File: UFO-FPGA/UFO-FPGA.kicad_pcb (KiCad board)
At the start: 2 copper layers, 68.6 x 53.3 mm, 12 parts, among them J1 Power, J2 Analog, J3 Digital/PWM, J4 Digital/PWM, U1 ICE40HX8K-BG121, U2 FT2232HL, U3 ASDMB-12MHz

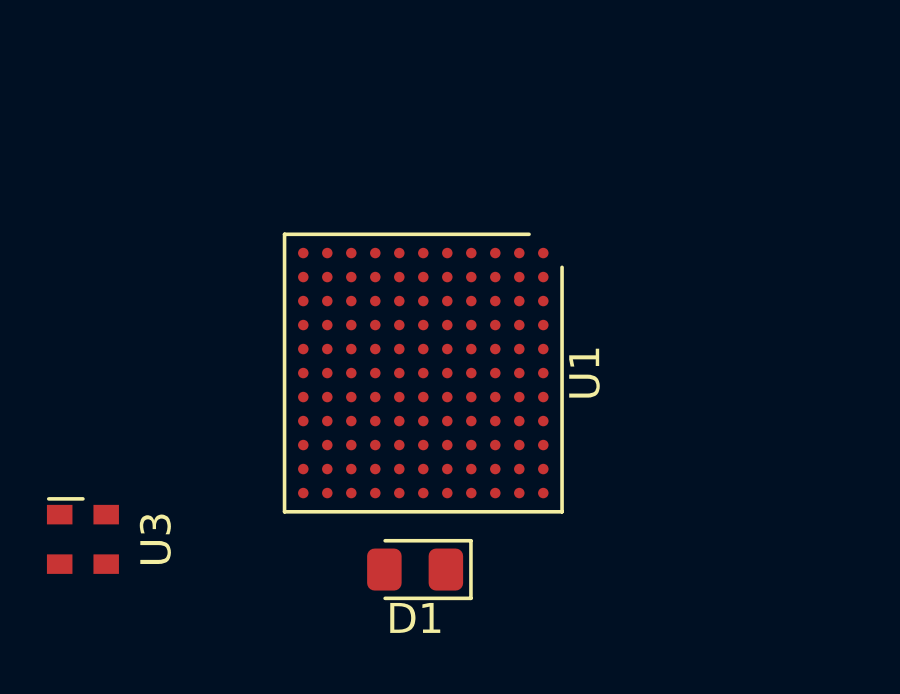
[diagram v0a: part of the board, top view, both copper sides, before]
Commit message: pins and USB
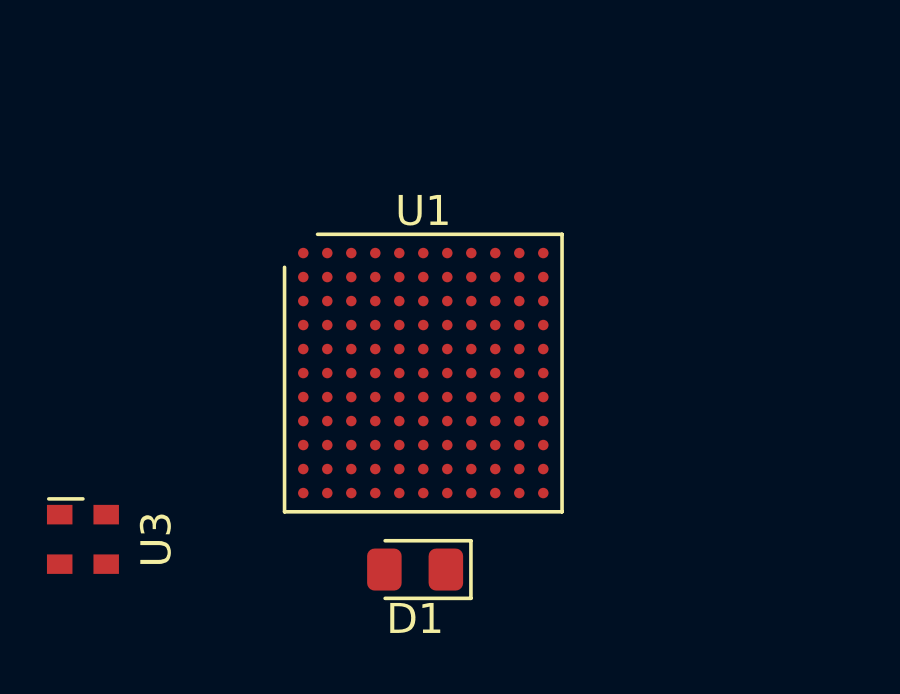
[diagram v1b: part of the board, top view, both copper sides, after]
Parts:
- turned U1 to 0 degrees
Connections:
- U1 pad A4: unconnected-(U1A-IOT_211-PadA4) -> MISO
- U1 pad A5: CHSEL -> ADC-CS
- U1 pad A6: ADC-CS -> SCK
- U1 pad B5: MISO -> CHSEL
- U1 pad B6: SCK -> unconnected-(U1A-IOT_198_GBIN0-PadB6)
- U1 pad G1: unconnected-(U1D-IOL_14A_GBIN6-PadG1) -> ICE_CLK

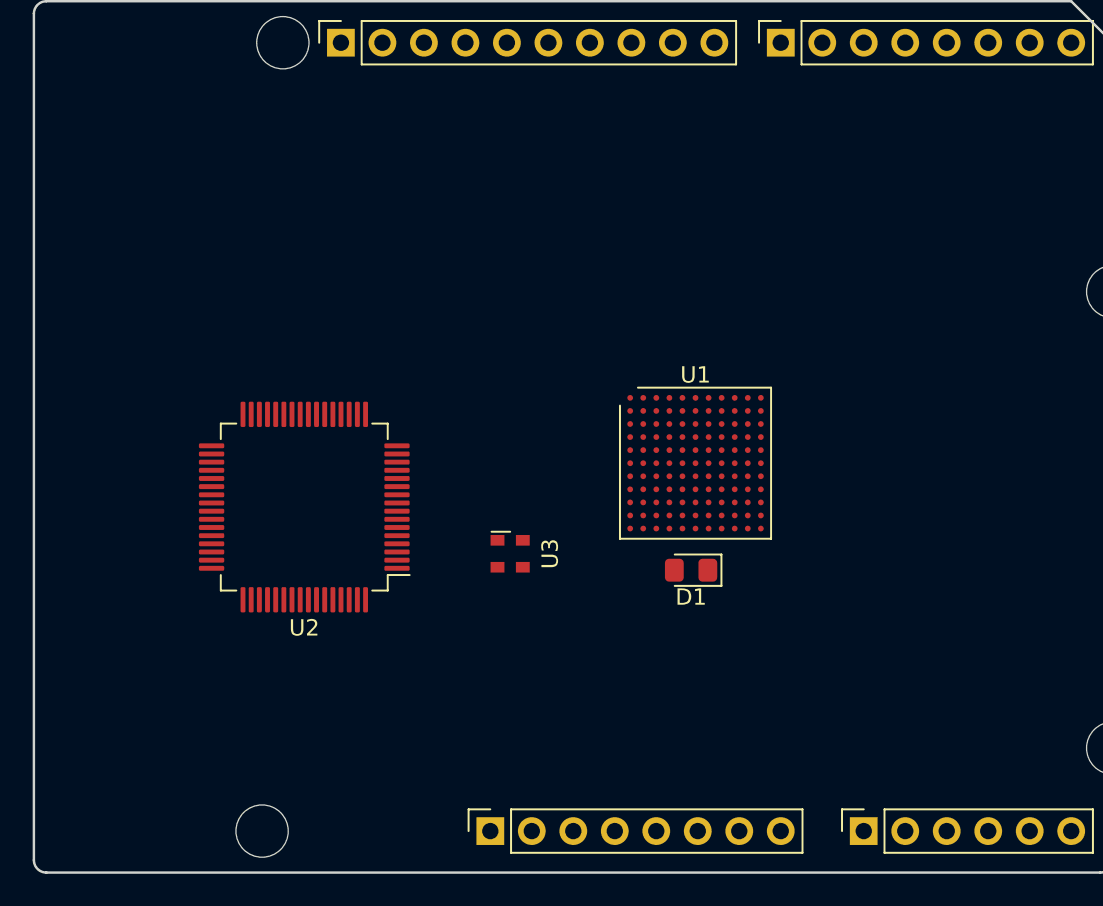
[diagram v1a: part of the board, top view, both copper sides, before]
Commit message: PCB and footprint
Added foorprints and moved on pcb layout
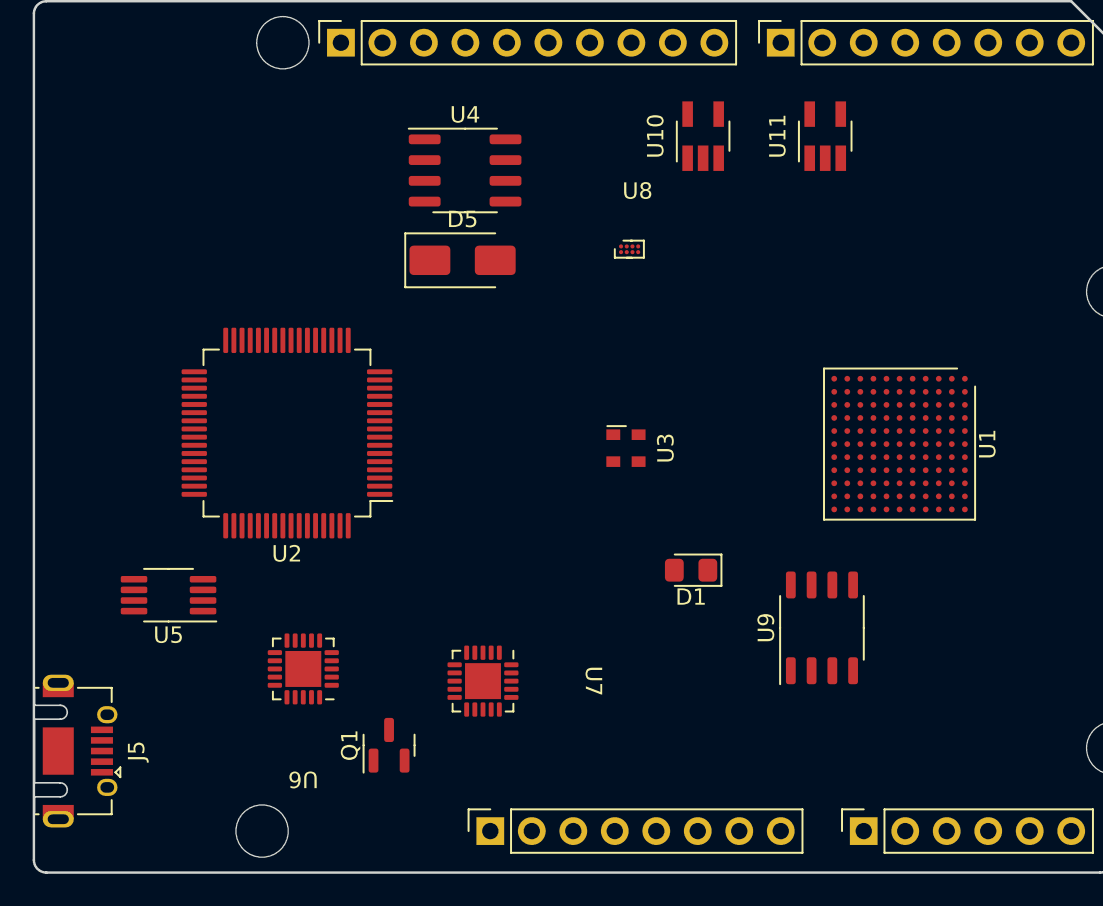
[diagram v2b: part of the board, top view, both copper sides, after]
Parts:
- added D5: B140-E3, Diode_SMD:D_SMA, F.Cu at (137.8, 64.0)
- added J5: USB_B_Micro, Connector_USB:USB_Micro-AB_Molex_47590-0001, F.Cu at (113.0, 94.0)
- added Q1: 2N7002, Package_TO_SOT_SMD:SOT-23, F.Cu at (133.2, 93.7)
- added U10: TL071, Package_TO_SOT_SMD:SOT-23-5_HandSoldering, F.Cu at (152.5, 56.4)
- added U11: TL071, Package_TO_SOT_SMD:SOT-23-5_HandSoldering, F.Cu at (159.9, 56.4)
- added U4: MC34063AD, Package_SO:SOIC-8_3.9x4.9mm_P1.27mm, F.Cu at (137.9, 58.5)
- added U5: 93LC56CT-I/MS, Package_SO:MSOP-8_3x3mm_P0.65mm, F.Cu at (119.8, 84.5)
- added U6: PWR convert, UFO-Footpints:W-QFN3535-20, F.Cu at (128.0, 95.3)
- added U7: PWR convert, UFO-Footpints:W-QFN3535-20, F.Cu at (145.3, 89.8)
- added U8: ADC, UFO-Footpints:WLP-8, F.Cu at (152.1, 57.2)
- added U9: N25Q032A13ESC40F, Package_SO:SOP-8_3.9x4.9mm_P1.27mm, F.Cu at (159.8, 86.5)
- J2: value Analog -> Digital
- J4: value Digital/PWM -> Digital
- moved U1 12.5 mm to (164.5, 75.2), turned to -90 degrees
- moved U3 9.59 mm to (147.8, 75.5)
- moved U2 4.65 mm to (127.0, 74.6)
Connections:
- net /USB Programmer/Prog-REF renamed Net-(U2-REF)
- net /USB Programmer/Prog-RESET renamed Net-(U2-~{RESET})
- J1 pad 2: /PINOUT/IOREF -> PIN-22
- J1 pad 3: /PINOUT/~{RESET} -> PIN-23
- J1 pad 8: VCC -> Vin
- J2 pad 1: /PINOUT/A0 -> PIN-18
- J2 pad 2: /PINOUT/A1 -> PIN-19
- J2 pad 3: /PINOUT/A2 -> PIN-20
- J2 pad 4: /PINOUT/A3 -> PIN-21
- J2 pad 5: /PINOUT/SDA/A4 -> AIN1
- J2 pad 6: /PINOUT/SCL/A5 -> AIN2
- J3 pad 1: /PINOUT/SCL/A5 -> PIN-1
- J3 pad 2: /PINOUT/SDA/A4 -> PIN-2
- J3 pad 3: /PINOUT/AREF -> PIN-3
- J3 pad 5: /PINOUT/13 -> PIN-4
- J3 pad 6: /PINOUT/12 -> PIN-5
- J4 pad 1: /PINOUT/7 -> PIN-10
- J4 pad 2: /PINOUT/*6 -> PIN-11
- J4 pad 3: /PINOUT/*5 -> PIN-12
- J4 pad 4: /PINOUT/4 -> PIN-13
- J4 pad 5: /PINOUT/*3 -> PIN-14
- J4 pad 6: /PINOUT/2 -> PIN-15
- J4 pad 7: /PINOUT/TX/1 -> PIN-16
- J4 pad 8: /PINOUT/RX/0 -> PIN-17
- U1 pad A1: unconnected-(U1A-IOT_225-PadA1) -> PIN-1
- U1 pad A10: RS232_Tx_TTL -> unconnected-(U1A-IOT_170-PadA10)
- U1 pad A11: RS232_Rx_TTL -> unconnected-(U1A-IOT_168-PadA11)
- U1 pad A2: unconnected-(U1A-IOT_222-PadA2) -> PIN-3
- U1 pad A3: unconnected-(U1A-IOT_223-PadA3) -> PIN-2
- U1 pad A7: DCDn -> unconnected-(U1A-IOT_192-PadA7)
- U1 pad A8: DSRn -> unconnected-(U1A-IOT_190-PadA8)
- U1 pad A9: DTRn -> unconnected-(U1A-IOT_178-PadA9)
- U1 pad B1: unconnected-(U1D-IOL_2A-PadB1) -> PIN-9
- U1 pad B11: unconnected-(U1B-IOR_161-PadB11) -> PIN-23
- U1 pad B2: unconnected-(U1D-IOL_2B-PadB2) -> PIN-8
- U1 pad B3: unconnected-(U1A-IOT_221-PadB3) -> PIN-4
- U1 pad B4: unconnected-(U1A-IOT_219-PadB4) -> PIN-5
- U1 pad B6: unconnected-(U1A-IOT_198_GBIN0-PadB6) -> PIN-6
- U1 pad B7: unconnected-(U1A-IOT_197_GBIN1-PadB7) -> PIN-7
- U1 pad B8: CTSn -> unconnected-(U1A-IOT_177-PadB8)
- U1 pad B9: RTSn -> unconnected-(U1A-IOT_174-PadB9)
- U1 pad C11: unconnected-(U1B-IOR_160-PadC11) -> PIN-22
- U1 pad D11: unconnected-(U1B-IOR_152-PadD11) -> PIN-21
- U1 pad E10: unconnected-(U1B-IOR_141_GBIN2-PadE10) -> PIN-19
- U1 pad E11: unconnected-(U1B-IOR_148-PadE11) -> PIN-20
- U1 pad F10: unconnected-(U1B-IOR_136-PadF10) -> PIN-17
- U1 pad F11: unconnected-(U1B-IOR_140_GBIN3-PadF11) -> PIN-18
- U1 pad G10: unconnected-(U1B-IOR_120-PadG10) -> PIN-15
- U1 pad G11: unconnected-(U1B-IOR_129-PadG11) -> PIN-16
- U1 pad H10: unconnected-(U1B-IOR_116-PadH10) -> PIN-12
- U1 pad H11: unconnected-(U1B-IOR_119-PadH11) -> PIN-14
- U1 pad J10: unconnected-(U1B-IOR_117-PadJ10) -> PIN-13
- U1 pad J11: unconnected-(U1B-IOR_114-PadJ11) -> PIN-10
- U1 pad K1: unconnected-(U1D-IOL_23B-PadK1) -> RS232_Tx_TTL
- U1 pad K11: unconnected-(U1B-IOR_115-PadK11) -> PIN-11
- U1 pad L1: unconnected-(U1C-IOB_56-PadL1) -> RS232_Rx_TTL
- U1 pad L2: unconnected-(U1C-IOB_61-PadL2) -> RTSn
- U1 pad L3: unconnected-(U1C-IOB_71-PadL3) -> CTSn
- U1 pad L4: unconnected-(U1C-IOB_72-PadL4) -> DTRn
- U1 pad L5: unconnected-(U1C-IOB_81_GBIN5-PadL5) -> DSRn
- U1 pad L7: unconnected-(U1C-IOB_94-PadL7) -> DCDn

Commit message: edge cuts
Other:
- outline, holes or cut-outs redrawn
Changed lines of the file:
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@@
   )
   (footprint "Connector_USB:USB_Micro-AB_Molex_47590-0001" (layer "F.Cu")
-    (at 113 94.041 -90)
+    (at 112.951 94.041 -90)
     (descr "Micro USB AB receptable, right-angle inverted (https://www.molex.com/pdm_docs/sd/475900001_sd.pdf)")
     (tags "Micro AB USB SMD")
@@
   (gr_line (start 180.088 63.38) (end 180.088 97.67)
     (stroke (width 0.15) (type solid)) (layer "Edge.Cuts"))
-  (gr_line (start 111.508 100.718) (end 111.508 48.902)
+  (gr_line (start 111.508 100.718) (end 111.506 97.791)
     (stroke (width 0.15) (type solid)) (layer "Edge.Cuts"))
   (gr_line (start 177.548 100.21) (end 177.548 100.718)
@@
   (gr_arc (start 112.27 101.48) (mid 111.731185 101.256815) (end 111.508 100.718)
     (stroke (width 0.15) (type solid)) (layer "Edge.Cuts"))
+  (gr_line (start 111.501 90.291) (end 111.508 48.902)
+    (stroke (width 0.15) (type solid)) (layer "Edge.Cuts"))
   (gr_line (start 112.27 48.14) (end 175.008 48.14)

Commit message: footprints and PCB
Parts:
- added D2: GREEN, LED_SMD:LED_0805_2012Metric_Pad1.15x1.40mm_HandSolder, F.Cu at (37.5, 85.6)
- added D3: RXLED, LED_SMD:LED_0805_2012Metric_Pad1.15x1.40mm_HandSolder, F.Cu at (33.1, 71.6)
- added D4: TXLED, LED_SMD:LED_0805_2012Metric_Pad1.15x1.40mm_HandSolder, F.Cu at (33.1, 74.6)
- added D6: LED, LED_SMD:LED_0805_2012Metric_Pad1.15x1.40mm_HandSolder, F.Cu at (44.3, 79.7)
- added D7: POWER, LED_SMD:LED_0805_2012Metric_Pad1.15x1.40mm_HandSolder, F.Cu at (63.2, 53.9)
- added FB1: 600 Ohm, 500mA, Inductor_SMD:L_1206_3216Metric_Pad1.22x1.90mm_HandSolder, F.Cu at (59.5, 71.5)
- added R1: 2K2, Resistor_SMD:R_0805_2012Metric_Pad1.20x1.40mm_HandSolder, F.Cu at (33.1, 53.8)
- added R10: 0, Resistor_SMD:R_0805_2012Metric_Pad1.20x1.40mm_HandSolder, F.Cu at (37.8, 62.7)
- added R11: 0, Resistor_SMD:R_0805_2012Metric_Pad1.20x1.40mm_HandSolder, F.Cu at (37.8, 65.6)
- added R12: 0, Resistor_SMD:R_0805_2012Metric_Pad1.20x1.40mm_HandSolder, F.Cu at (37.8, 68.6)
- added R13: 0, Resistor_SMD:R_0805_2012Metric_Pad1.20x1.40mm_HandSolder, F.Cu at (42.6, 53.8)
- added R14: 0, Resistor_SMD:R_0805_2012Metric_Pad1.20x1.40mm_HandSolder, F.Cu at (42.6, 56.8)
- added R15: 0, Resistor_SMD:R_0805_2012Metric_Pad1.20x1.40mm_HandSolder, F.Cu at (42.6, 59.7)
- added R16: 0, Resistor_SMD:R_0805_2012Metric_Pad1.20x1.40mm_HandSolder, F.Cu at (42.6, 62.7)
- added R17: 0, Resistor_SMD:R_0805_2012Metric_Pad1.20x1.40mm_HandSolder, F.Cu at (42.6, 65.6)
- added R18: 0, Resistor_SMD:R_0805_2012Metric_Pad1.20x1.40mm_HandSolder, F.Cu at (42.6, 68.6)
- added R19: 0, Resistor_SMD:R_0805_2012Metric_Pad1.20x1.40mm_HandSolder, F.Cu at (47.3, 53.8)
- added R2: 10K, Resistor_SMD:R_0805_2012Metric_Pad1.20x1.40mm_HandSolder, F.Cu at (33.1, 56.8)
- added R20: 0, Resistor_SMD:R_0805_2012Metric_Pad1.20x1.40mm_HandSolder, F.Cu at (47.3, 56.8)
- added R21: 10K, Resistor_SMD:R_0805_2012Metric_Pad1.20x1.40mm_HandSolder, F.Cu at (54.1, 79.4)
- added R22: 10K, Resistor_SMD:R_0805_2012Metric_Pad1.20x1.40mm_HandSolder, F.Cu at (54.1, 82.4)
- added R23: 10K, Resistor_SMD:R_0805_2012Metric_Pad1.20x1.40mm_HandSolder, F.Cu at (54.1, 85.3)
- added R24: 10K, Resistor_SMD:R_0805_2012Metric_Pad1.20x1.40mm_HandSolder, F.Cu at (54.1, 88.3)
- added R25: 100, Resistor_SMD:R_0805_2012Metric_Pad1.20x1.40mm_HandSolder, F.Cu at (54.1, 91.2)
- added R26: 100, Resistor_SMD:R_0805_2012Metric_Pad1.20x1.40mm_HandSolder, F.Cu at (54.1, 94.2)
- added R27: 10K, Resistor_SMD:R_0805_2012Metric_Pad1.20x1.40mm_HandSolder, F.Cu at (37.4, 79.6)
- added R29: 1, Resistor_SMD:R_0805_2012Metric_Pad1.20x1.40mm_HandSolder, F.Cu at (37.4, 82.6)
- added R3: 10K, Resistor_SMD:R_0805_2012Metric_Pad1.20x1.40mm_HandSolder, F.Cu at (33.1, 59.7)
- added R30: 1, Resistor_SMD:R_0805_2012Metric_Pad1.20x1.40mm_HandSolder, F.Cu at (46.6, 90.5)
- added R31: 1, Resistor_SMD:R_0805_2012Metric_Pad1.20x1.40mm_HandSolder, F.Cu at (33.1, 90.5)
- added R32: 1, Resistor_SMD:R_0805_2012Metric_Pad1.20x1.40mm_HandSolder, F.Cu at (39.8, 90.5)
- added R33: 220R, Resistor_SMD:R_0805_2012Metric_Pad1.20x1.40mm_HandSolder, F.Cu at (47.3, 59.7)
- added R34: 220R, Resistor_SMD:R_0805_2012Metric_Pad1.20x1.40mm_HandSolder, F.Cu at (47.3, 62.7)
- added R35: 0, Resistor_SMD:R_0805_2012Metric_Pad1.20x1.40mm_HandSolder, F.Cu at (54.1, 53.8)
- added R36: 1K, Resistor_SMD:R_0805_2012Metric_Pad1.20x1.40mm_HandSolder, F.Cu at (54.1, 56.8)
- added R37: 12K4, Resistor_SMD:R_0805_2012Metric_Pad1.20x1.40mm_HandSolder, F.Cu at (54.1, 59.7)
- added R38: 24K9, Resistor_SMD:R_0805_2012Metric_Pad1.20x1.40mm_HandSolder, F.Cu at (54.1, 62.7)
- added R39: 100k, Resistor_SMD:R_0805_2012Metric_Pad1.20x1.40mm_HandSolder, F.Cu at (54.1, 65.6)
- added R4: 10K, Resistor_SMD:R_0805_2012Metric_Pad1.20x1.40mm_HandSolder, F.Cu at (33.1, 62.7)
- added R40: 1M, Resistor_SMD:R_0805_2012Metric_Pad1.20x1.40mm_HandSolder, F.Cu at (54.1, 68.6)
- added R41: 1M, Resistor_SMD:R_0805_2012Metric_Pad1.20x1.40mm_HandSolder, F.Cu at (54.1, 71.5)
- added R5: 2K2, Resistor_SMD:R_0805_2012Metric_Pad1.20x1.40mm_HandSolder, F.Cu at (33.1, 65.6)
- added R55: 1M, Resistor_SMD:R_0805_2012Metric_Pad1.20x1.40mm_HandSolder, F.Cu at (54.1, 74.5)
- added R6: 12K, Resistor_SMD:R_0805_2012Metric_Pad1.20x1.40mm_HandSolder, F.Cu at (33.1, 68.6)
- added R7: 0, Resistor_SMD:R_0805_2012Metric_Pad1.20x1.40mm_HandSolder, F.Cu at (37.8, 53.8)
- added R8: 0, Resistor_SMD:R_0805_2012Metric_Pad1.20x1.40mm_HandSolder, F.Cu at (37.8, 56.8)
- added R9: 0, Resistor_SMD:R_0805_2012Metric_Pad1.20x1.40mm_HandSolder, F.Cu at (37.8, 59.7)
- added SW2: SW_DIP_x01, Button_Switch_SMD:SW_DIP_SPSTx01_Slide_9.78x4.72mm_W8.61mm_P2.54mm, F.Cu at (62.8, 81.2)
- added TP1: TestPoint, TestPoint:TestPoint_Keystone_5000-5004_Miniature, F.Cu at (58.6, 54.5)
- added TP10: TestPoint, TestPoint:TestPoint_Keystone_5000-5004_Miniature, F.Cu at (32.9, 94.2)
- added TP11: TestPoint, TestPoint:TestPoint_Keystone_5000-5004_Miniature, F.Cu at (39.6, 94.2)
- added TP12: TestPoint, TestPoint:TestPoint_Keystone_5000-5004_Miniature, F.Cu at (58.6, 67.6)
- added TP13: TestPoint, TestPoint:TestPoint_Keystone_5000-5004_Miniature, F.Cu at (44.0, 83.3)
- added TP2: TestPoint, TestPoint:TestPoint_Keystone_5000-5004_Miniature, F.Cu at (58.6, 58.9)
- added TP3: TestPoint, TestPoint:TestPoint_Keystone_5000-5004_Miniature, F.Cu at (58.6, 63.2)
- added TP4: TestPoint, TestPoint:TestPoint_Keystone_5000-5004_Miniature, F.Cu at (58.6, 86.6)
- added TP5: TestPoint, TestPoint:TestPoint_Keystone_5000-5004_Miniature, F.Cu at (58.6, 90.9)
- added TP6: TestPoint, TestPoint:TestPoint_Keystone_5000-5004_Miniature, F.Cu at (58.6, 95.3)
- added TP7: TestPoint, TestPoint:TestPoint_Keystone_5000-5004_Miniature, F.Cu at (32.9, 80.3)
- added TP8: TestPoint, TestPoint:TestPoint_Keystone_5000-5004_Miniature, F.Cu at (32.9, 84.7)
- added TP9: TestPoint, TestPoint:TestPoint_Keystone_5000-5004_Miniature, F.Cu at (46.4, 94.2)
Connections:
- U6 pad 14: +5V -> Net-(U6-EN)
